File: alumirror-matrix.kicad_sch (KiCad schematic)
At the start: 54 parts, among them K00 PG1350, K01 PG1350, K02 PG1350, K03 PG1350, K04 PG1350, K05 PG1350, K10 PG1350, K11 PG1350, K12 PG1350, K13 PG1350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

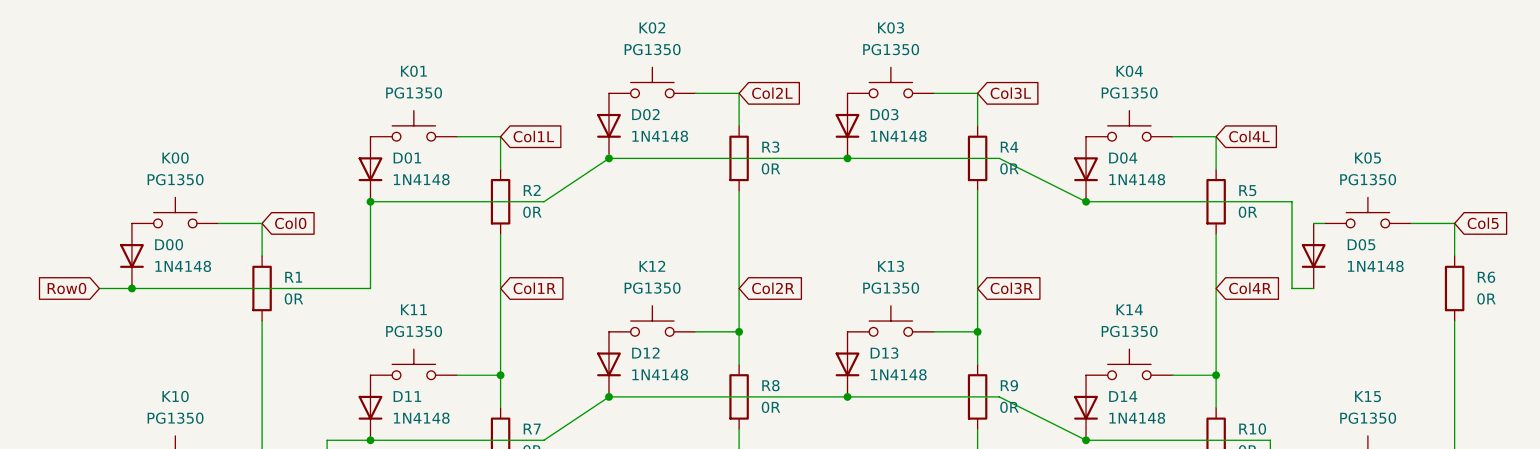
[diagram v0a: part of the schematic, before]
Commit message: Refine middle layer 3D print cutouts
Also renumber diodes — D0# are now DO# and SD1 and SD2 are and D2
Add diode (D3) on VCC line to RGB LED (this drops VCC to ~4V, which is still within spec., but now closer to the 3.3V control signal as DIN should be VCC±0.5V).
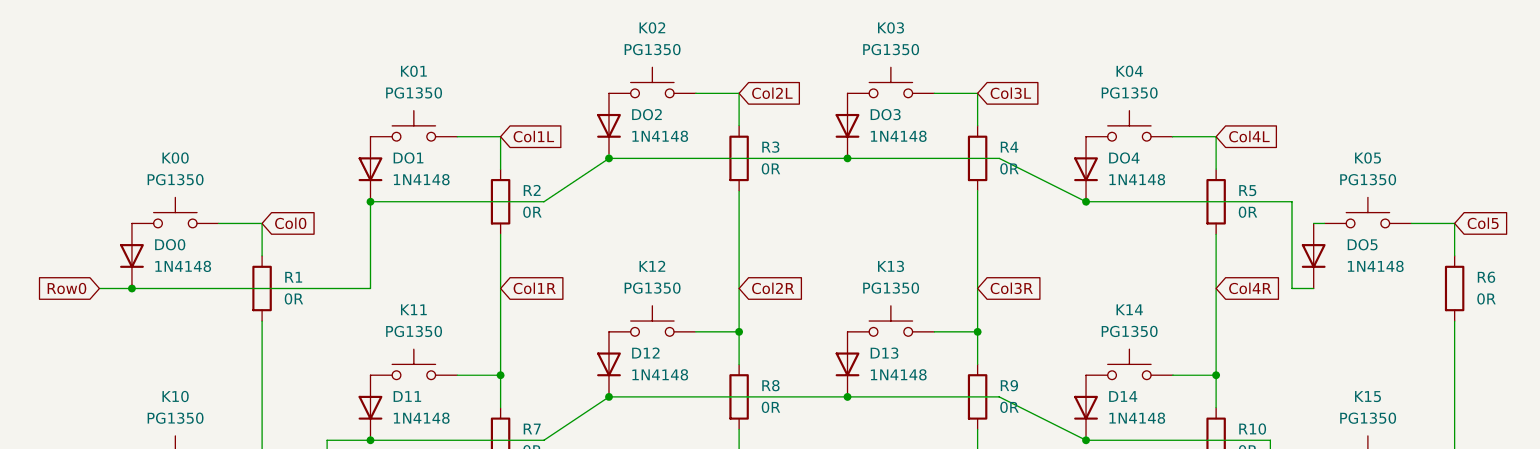
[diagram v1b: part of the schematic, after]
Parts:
- D30, D31, D32, D33, D34, D35: footprint Project Library:D_SOD-123_Mod -> Diode_SMD:D_SOD-123
- renumbered D00 to DO0, D01 to DO1, D02 to DO2, D03 to DO3, D04 to DO4, D05 to DO5
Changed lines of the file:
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@@
 			)
 		)
-		(property "Footprint" "Project Library:D_SOD-123_Mod"
+		(property "Footprint" "Diode_SMD:D_SOD-123"
 			(at 77.47 161.29 0)
 			(effects
@@
 		(dnp no)
 		(fields_autoplaced yes)
-		(property "Reference" "D01"
+		(property "Reference" "DO1"
 			(at 102.87 45.7199 90)
 			(effects
@@
 			(project "alumirror"
 				(path "/52f043ac-ccff-4c85-bc10-2db9d3c9e3f3/ba0213d9-9934-4194-9bec-bf394cd27126"
-					(reference "D01")
+					(reference "DO1")
 					(unit 1)
 				)
@@
 			)
 		)
-		(property "Footprint" "Project Library:D_SOD-123_Mod"
+		(property "Footprint" "Diode_SMD:D_SOD-123"
 			(at 77.47 151.13 0)
 			(effects
@@
 			)
 		)
-		(property "Footprint" "Project Library:D_SOD-123_Mod"
+		(property "Footprint" "Diode_SMD:D_SOD-123"
 			(at 77.47 166.37 0)
 			(effects
@@
 		(dnp no)
 		(fields_autoplaced yes)
-		(property "Reference" "D04"
+		(property "Reference" "DO4"
 			(at 186.69 45.7199 90)
 			(effects
@@
 			(project "alumirror"
 				(path "/52f043ac-ccff-4c85-bc10-2db9d3c9e3f3/ba0213d9-9934-4194-9bec-bf394cd27126"
-					(reference "D04")
+					(reference "DO4")
 					(unit 1)
 				)
@@
 		(on_board yes)
 		(dnp no)
-		(property "Reference" "D05"
+		(property "Reference" "DO5"
 			(at 214.63 55.8799 90)
 			(effects
@@
 			(project "alumirror"
 				(path "/52f043ac-ccff-4c85-bc10-2db9d3c9e3f3/ba0213d9-9934-4194-9bec-bf394cd27126"
-					(reference "D05")
+					(reference "DO5")
 					(unit 1)
 				)
@@
 			)
 		)
-		(property "Footprint" "Project Library:D_SOD-123_Mod"
+		(property "Footprint" "Diode_SMD:D_SOD-123"
 			(at 44.45 152.4 0)
 			(effects
@@
 		(dnp no)
 		(fields_autoplaced yes)
-		(property "Reference" "D02"
+		(property "Reference" "DO2"
 			(at 130.81 40.6399 90)
 			(effects
@@
 			(project "alumirror"
 				(path "/52f043ac-ccff-4c85-bc10-2db9d3c9e3f3/ba0213d9-9934-4194-9bec-bf394cd27126"
-					(reference "D02")
+					(reference "DO2")
 					(unit 1)
 				)
@@
 		(dnp no)
 		(fields_autoplaced yes)
-		(property "Reference" "D00"
+		(property "Reference" "DO0"
 			(at 74.93 55.8799 90)
 			(effects
@@
 			(project "alumirror"
 				(path "/52f043ac-ccff-4c85-bc10-2db9d3c9e3f3/ba0213d9-9934-4194-9bec-bf394cd27126"
-					(reference "D00")
+					(reference "DO0")
 					(unit 1)
 				)
@@
 			)
 		)
-		(property "Footprint" "Project Library:D_SOD-123_Mod"
+		(property "Footprint" "Diode_SMD:D_SOD-123"
 			(at 77.47 146.05 0)
 			(effects
@@
 			)
 		)
-		(property "Footprint" "Project Library:D_SOD-123_Mod"
+		(property "Footprint" "Diode_SMD:D_SOD-123"
 			(at 77.47 156.21 0)
 			(effects
@@
 		(dnp no)
 		(fields_autoplaced yes)
-		(property "Reference" "D03"
+		(property "Reference" "DO3"
 			(at 158.75 40.6399 90)
 			(effects
@@
 			(project "alumirror"
 				(path "/52f043ac-ccff-4c85-bc10-2db9d3c9e3f3/ba0213d9-9934-4194-9bec-bf394cd27126"
-					(reference "D03")
+					(reference "DO3")
 					(unit 1)
 				)

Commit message: Create another custom SOD-123 footprint
This one has the thicker polarity line of the existing modification, but without the 3D layer cutout.
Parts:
- D30, D31, D32, D33, D34, D35: footprint Diode_SMD:D_SOD-123 -> Project Library:D_SOD-123
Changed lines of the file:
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@@
 			)
 		)
-		(property "Footprint" "Diode_SMD:D_SOD-123"
+		(property "Footprint" "Project Library:D_SOD-123"
 			(at 77.47 161.29 0)
 			(effects
@@
 			)
 		)
-		(property "Footprint" "Diode_SMD:D_SOD-123"
+		(property "Footprint" "Project Library:D_SOD-123"
 			(at 77.47 151.13 0)
 			(effects
@@
 			)
 		)
-		(property "Footprint" "Diode_SMD:D_SOD-123"
+		(property "Footprint" "Project Library:D_SOD-123"
 			(at 77.47 166.37 0)
 			(effects
@@
 			)
 		)
-		(property "Footprint" "Diode_SMD:D_SOD-123"
+		(property "Footprint" "Project Library:D_SOD-123"
 			(at 44.45 152.4 0)
 			(effects
@@
 			)
 		)
-		(property "Footprint" "Diode_SMD:D_SOD-123"
+		(property "Footprint" "Project Library:D_SOD-123"
 			(at 77.47 146.05 0)
 			(effects
@@
 			)
 		)
-		(property "Footprint" "Diode_SMD:D_SOD-123"
+		(property "Footprint" "Project Library:D_SOD-123"
 			(at 77.47 156.21 0)
 			(effects

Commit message: Add identifying text to PCB
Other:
- company: (none) -> bgkendall
- title: (none) -> Alumirror 
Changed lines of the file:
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@@
 	(paper "A4")
 	(title_block
-		(comment 1 "Key switch matrix")
+		(title "Alumirror ")
+		(rev "0.1")
+		(company "bgkendall")
+		(comment 1 "Split one-layer reversible keyboard PCB")
+		(comment 2 "Key switch matrix for")
 	)
 	(junction
